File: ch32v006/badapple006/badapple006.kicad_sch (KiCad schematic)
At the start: 25 parts, among them J1 OLED, J2 USB_C_Receptacle_USB2.0, J3 PG, J4 3v3, J5 GND, J6 RFO, J7 RFA, J8 APPLE, U1 CH32V006F8U6, U2 XC6206P332, Y1 24MHz

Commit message: Bump design
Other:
- moved on the sheet: C6, U2

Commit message: Bump design
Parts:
- removed U2: XC6206P332, Package_TO_SOT_SMD:SOT-23, symbol Regulator_Linear:IFX27001TFV26
- added D1: D_Schottky, Diode_SMD:D_SOD-323, symbol Device:D_Schottky
- added J10: 3v3, TestPoint:TestPoint_Pad_D1.0mm, symbol Connector_Generic:Conn_01x01
- added J11: GND, TestPoint:TestPoint_Pad_D1.0mm, symbol Connector_Generic:Conn_01x01
- added J9: PG, TestPoint:TestPoint_Pad_D1.0mm, symbol Connector_Generic:Conn_01x01
- added L1: 4.7uH, Inductor_SMD:L_0603_1608Metric, symbol Device:L
- added R5: 62k, Resistor_SMD:R_0402_1005Metric, symbol Device:R
- added R6: 5.1k, Resistor_SMD:R_0402_1005Metric, symbol Device:R
- added U2: MT3540, Package_TO_SOT_SMD:SOT-23-5, symbol cnhardware:MT3540
- added U3: RS3236-3.3YUTDN4, cnhardware:xdfn-reg, symbol cnhardware:RS3236-DFN-LDO
- C5: value 2.2u16v -> 4.7u10v; LCSC C72203 -> C23733
- C6: value 4.7u16v -> 4.7u10v; footprint Capacitor_SMD:C_0603_1608Metric -> Capacitor_SMD:C_0402_1005Metric; LCSC C77045 -> C23733
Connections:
- net GND: now also J11.1 (Pin_1), R6.1, U2.2 (GND), U3.2 (GND), U3.5 (FLAG_GND)
- net SWIO: now also J9.1 (Pin_1)
- net VBUS: now also C5.1, L1.2, U2.4 (EN), U2.5 (VIN), U3.3 (EN), U3.4 (IN)
- net VDD: now also J1.2 (Pin_2), R4.1, J10.1 (Pin_1), U3.1 (OUT)
- net OLEDVCC: now reaches C2.1, C3.1, J1.8 (Pin_8)
- net OLEDVCC: now also D1.1 (K), R5.2
- net DPU: no longer names the net of U1.19 (PD5/T2/TX/RX_/MISO_/A5)
- net DPU: no longer R4.1
- removed net OVDD: C5.1, J1.2 (Pin_2), U1.11 (PC4/T1C1_/T1/MCO/A2)
- new net: R5.1, R6.2, U2.3 (FB)
- new net: D1.2 (A), L1.1, U2.1 (SW)
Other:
- moved on the sheet: C1, R1

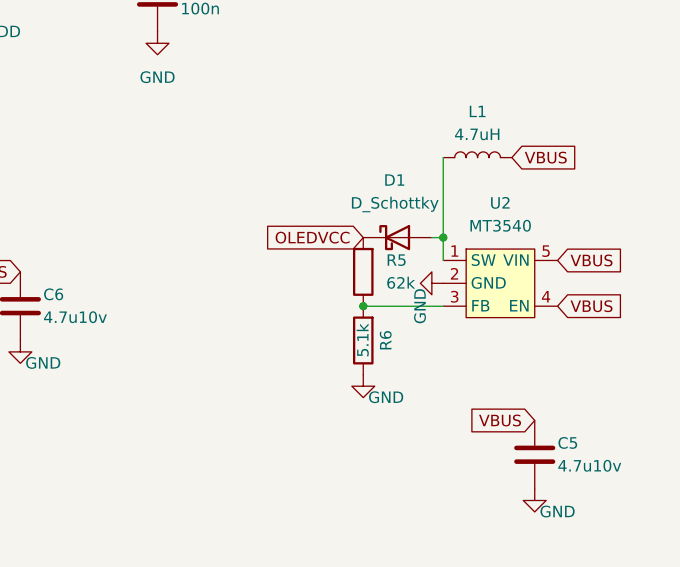
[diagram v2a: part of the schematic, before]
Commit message: Bump design to have correct voltage on feedback
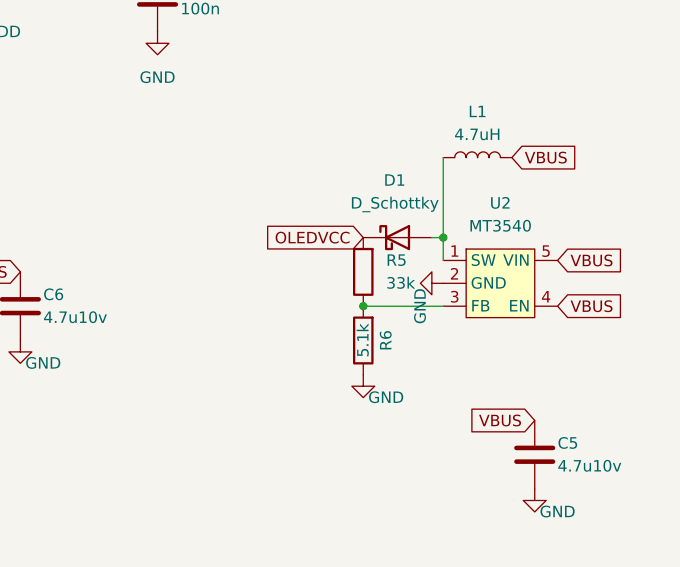
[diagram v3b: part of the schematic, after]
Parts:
- R5: value 62k -> 33k; LCSC C37825 -> C25779
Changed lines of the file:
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@@
 			)
 		)
-		(property "Value" "62k"
+		(property "Value" "33k"
 			(at 231.14 107.9499 0)
 			(effects
@@
 			)
 		)
-		(property "LCSC" "C37825"
+		(property "LCSC" "C25779"
 			(at 228.6 106.68 0)
 			(effects

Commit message: Switch to 27k
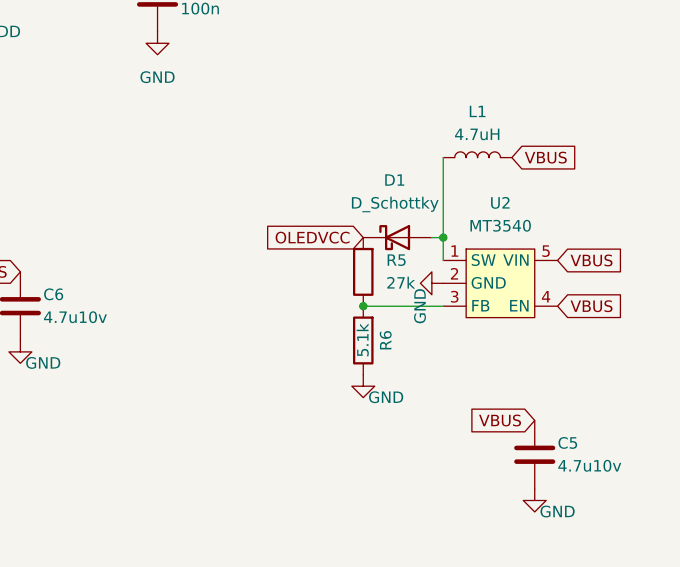
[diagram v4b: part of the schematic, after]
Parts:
- R5: value 33k -> 27k; LCSC C25779 -> C25771
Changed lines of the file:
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@@
 			)
 		)
-		(property "Value" "33k"
+		(property "Value" "27k"
 			(at 231.14 107.9499 0)
 			(effects
@@
 			)
 		)
-		(property "LCSC" "C25779"
+		(property "LCSC" "C25771"
 			(at 228.6 106.68 0)
 			(effects
